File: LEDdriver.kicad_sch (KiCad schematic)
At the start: 5 parts, among them Q30 LBSS84LT1G, Q31 2N7002

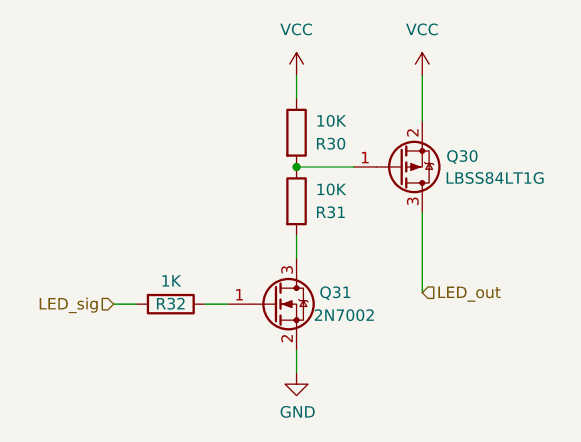
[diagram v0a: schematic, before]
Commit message: Converted Project name to Rotini + files ordered for V1
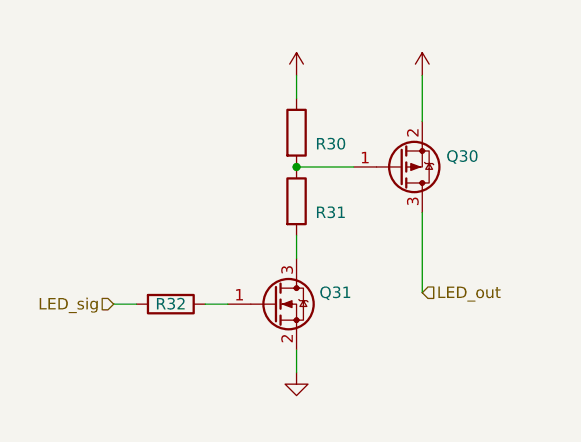
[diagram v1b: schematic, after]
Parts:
- Q30: value LBSS84LT1G -> (none); footprint Package_TO_SOT_SMD:SOT-23 -> (none)
- Q31: value 2N7002 -> (none); footprint Package_TO_SOT_SMD:SOT-23 -> (none)
- R30, R31: value 10K -> (none); footprint Resistor_SMD:R_0402_1005Metric -> (none)
- R32: value 1K -> (none); footprint Resistor_SMD:R_0402_1005Metric -> (none)
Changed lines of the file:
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@@
   (symbol (lib_id "power:VCC") (at 139.7 86.36 0) (unit 1)
     (in_bom yes) (on_board yes) (fields_autoplaced)
-    (property "Reference" "#PWR0175" (id 0) (at 139.7 90.17 0)
+    (property "Reference" "#PWR0152" (id 0) (at 139.7 90.17 0)
       (effects (font (size 1.27 1.27)) hide)
     )
-    (property "Value" "VCC" (id 1) (at 139.7 81.28 0))
+    (property "Value" "" (id 1) (at 139.7 81.28 0))
     (property "Footprint" "" (id 2) (at 139.7 86.36 0)
       (effects (font (size 1.27 1.27)) hide)
@@
       (effects (font (size 1.27 1.27)) (justify left))
     )
-    (property "Value" "2N7002" (id 1) (at 141.605 113.03 0)
+    (property "Value" "" (id 1) (at 141.605 113.03 0)
       (effects (font (size 1.27 1.27)) (justify left))
     )
-    (property "Footprint" "Package_TO_SOT_SMD:SOT-23" (id 2) (at 142.24 113.665 0)
+    (property "Footprint" "" (id 2) (at 142.24 113.665 0)
       (effects (font (size 1.27 1.27) italic) (justify left) hide)
     )
@@
     (in_bom yes) (on_board yes)
     (property "Reference" "R31" (id 0) (at 143.51 101.6 0))
-    (property "Value" "10K" (id 1) (at 143.51 99.06 0))
-    (property "Footprint" "Resistor_SMD:R_0402_1005Metric" (id 2) (at 137.922 100.33 90)
+    (property "Value" "" (id 1) (at 143.51 99.06 0))
+    (property "Footprint" "" (id 2) (at 137.922 100.33 90)
       (effects (font (size 1.27 1.27)) hide)
     )
@@
   (symbol (lib_id "power:GND") (at 139.7 119.38 0) (unit 1)
     (in_bom yes) (on_board yes)
-    (property "Reference" "#PWR0174" (id 0) (at 139.7 125.73 0)
+    (property "Reference" "#PWR0121" (id 0) (at 139.7 125.73 0)
       (effects (font (size 1.27 1.27)) hide)
     )
-    (property "Value" "GND" (id 1) (at 139.827 123.7742 0))
+    (property "Value" "" (id 1) (at 139.827 123.7742 0))
     (property "Footprint" "" (id 2) (at 139.7 119.38 0)
       (effects (font (size 1.27 1.27)) hide)
@@
       (effects (font (size 1.27 1.27)) (justify left))
     )
-    (property "Value" "LBSS84LT1G" (id 1) (at 156.21 97.79 0)
+    (property "Value" "" (id 1) (at 156.21 97.79 0)
       (effects (font (size 1.27 1.27)) (justify left))
     )
-    (property "Footprint" "Package_TO_SOT_SMD:SOT-23" (id 2) (at 156.21 94.615 0)
+    (property "Footprint" "" (id 2) (at 156.21 94.615 0)
       (effects (font (size 1.27 1.27) italic) (justify left) hide)
     )
@@
     (in_bom yes) (on_board yes)
     (property "Reference" "R30" (id 0) (at 143.51 93.98 0))
-    (property "Value" "10K" (id 1) (at 143.51 91.44 0))
-    (property "Footprint" "Resistor_SMD:R_0402_1005Metric" (id 2) (at 137.922 92.71 90)
+    (property "Value" "" (id 1) (at 143.51 91.44 0))
+    (property "Footprint" "" (id 2) (at 137.922 92.71 90)
       (effects (font (size 1.27 1.27)) hide)
     )
@@
     (in_bom yes) (on_board yes)
     (property "Reference" "R32" (id 0) (at 125.73 111.76 90))
-    (property "Value" "1K" (id 1) (at 125.73 109.22 90))
-    (property "Footprint" "Resistor_SMD:R_0402_1005Metric" (id 2) (at 125.73 109.982 90)
+    (property "Value" "" (id 1) (at 125.73 109.22 90))
+    (property "Footprint" "" (id 2) (at 125.73 109.982 90)
       (effects (font (size 1.27 1.27)) hide)
     )
@@
   (symbol (lib_id "power:VCC") (at 153.67 86.36 0) (unit 1)
     (in_bom yes) (on_board yes) (fields_autoplaced)
-    (property "Reference" "#PWR0176" (id 0) (at 153.67 90.17 0)
+    (property "Reference" "#PWR0122" (id 0) (at 153.67 90.17 0)
       (effects (font (size 1.27 1.27)) hide)
     )
-    (property "Value" "VCC" (id 1) (at 153.67 81.28 0))
+    (property "Value" "" (id 1) (at 153.67 81.28 0))
     (property "Footprint" "" (id 2) (at 153.67 86.36 0)
       (effects (font (size 1.27 1.27)) hide)

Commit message: First push with Rotini V2 features, removed CP210x USB circuit
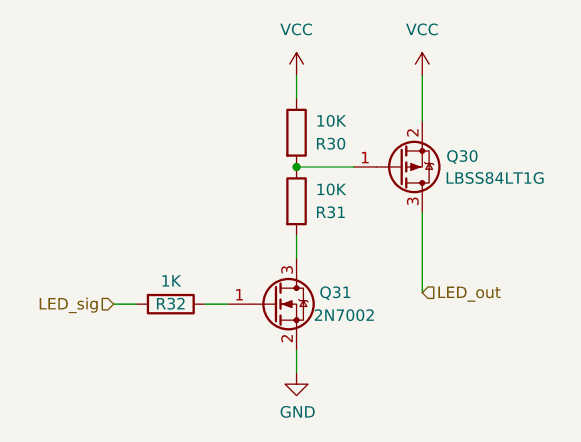
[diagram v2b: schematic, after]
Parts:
- Q30: value (none) -> LBSS84LT1G
- Q31: value (none) -> 2N7002
- R30, R31: value (none) -> 10K
- R32: value (none) -> 1K
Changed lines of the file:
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@@
       (effects (font (size 1.27 1.27)) hide)
     )
-    (property "Value" "" (id 1) (at 139.7 81.28 0))
+    (property "Value" "VCC" (id 1) (at 139.7 81.28 0))
     (property "Footprint" "" (id 2) (at 139.7 86.36 0)
       (effects (font (size 1.27 1.27)) hide)
@@
       (effects (font (size 1.27 1.27)) (justify left))
     )
-    (property "Value" "" (id 1) (at 141.605 113.03 0)
+    (property "Value" "2N7002" (id 1) (at 141.605 113.03 0)
       (effects (font (size 1.27 1.27)) (justify left))
     )
@@
     (in_bom yes) (on_board yes)
     (property "Reference" "R31" (id 0) (at 143.51 101.6 0))
-    (property "Value" "" (id 1) (at 143.51 99.06 0))
+    (property "Value" "10K" (id 1) (at 143.51 99.06 0))
     (property "Footprint" "" (id 2) (at 137.922 100.33 90)
       (effects (font (size 1.27 1.27)) hide)
@@
       (effects (font (size 1.27 1.27)) hide)
     )
-    (property "Value" "" (id 1) (at 139.827 123.7742 0))
+    (property "Value" "GND" (id 1) (at 139.827 123.7742 0))
     (property "Footprint" "" (id 2) (at 139.7 119.38 0)
       (effects (font (size 1.27 1.27)) hide)
@@
       (effects (font (size 1.27 1.27)) (justify left))
     )
-    (property "Value" "" (id 1) (at 156.21 97.79 0)
+    (property "Value" "LBSS84LT1G" (id 1) (at 156.21 97.79 0)
       (effects (font (size 1.27 1.27)) (justify left))
     )
@@
     (in_bom yes) (on_board yes)
     (property "Reference" "R30" (id 0) (at 143.51 93.98 0))
-    (property "Value" "" (id 1) (at 143.51 91.44 0))
+    (property "Value" "10K" (id 1) (at 143.51 91.44 0))
     (property "Footprint" "" (id 2) (at 137.922 92.71 90)
       (effects (font (size 1.27 1.27)) hide)
@@
     (in_bom yes) (on_board yes)
     (property "Reference" "R32" (id 0) (at 125.73 111.76 90))
-    (property "Value" "" (id 1) (at 125.73 109.22 90))
+    (property "Value" "1K" (id 1) (at 125.73 109.22 90))
     (property "Footprint" "" (id 2) (at 125.73 109.982 90)
       (effects (font (size 1.27 1.27)) hide)
@@
       (effects (font (size 1.27 1.27)) hide)
     )
-    (property "Value" "" (id 1) (at 153.67 81.28 0))
+    (property "Value" "VCC" (id 1) (at 153.67 81.28 0))
     (property "Footprint" "" (id 2) (at 153.67 86.36 0)
       (effects (font (size 1.27 1.27)) hide)

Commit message: Hardware bought of Rotini V2
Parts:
- Q30, Q31: footprint (none) -> Package_TO_SOT_SMD:SOT-23
- R30, R31, R32: footprint (none) -> Resistor_SMD:R_0402_1005Metric
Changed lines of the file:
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@@
       (effects (font (size 1.27 1.27)) (justify left))
     )
-    (property "Footprint" "" (id 2) (at 142.24 113.665 0)
+    (property "Footprint" "Package_TO_SOT_SMD:SOT-23" (id 2) (at 142.24 113.665 0)
       (effects (font (size 1.27 1.27) italic) (justify left) hide)
     )
@@
     (property "Reference" "R31" (id 0) (at 143.51 101.6 0))
     (property "Value" "10K" (id 1) (at 143.51 99.06 0))
-    (property "Footprint" "" (id 2) (at 137.922 100.33 90)
+    (property "Footprint" "Resistor_SMD:R_0402_1005Metric" (id 2) (at 137.922 100.33 90)
       (effects (font (size 1.27 1.27)) hide)
     )
@@
       (effects (font (size 1.27 1.27)) (justify left))
     )
-    (property "Footprint" "" (id 2) (at 156.21 94.615 0)
+    (property "Footprint" "Package_TO_SOT_SMD:SOT-23" (id 2) (at 156.21 94.615 0)
       (effects (font (size 1.27 1.27) italic) (justify left) hide)
     )
@@
     (property "Reference" "R30" (id 0) (at 143.51 93.98 0))
     (property "Value" "10K" (id 1) (at 143.51 91.44 0))
-    (property "Footprint" "" (id 2) (at 137.922 92.71 90)
+    (property "Footprint" "Resistor_SMD:R_0402_1005Metric" (id 2) (at 137.922 92.71 90)
       (effects (font (size 1.27 1.27)) hide)
     )
@@
     (property "Reference" "R32" (id 0) (at 125.73 111.76 90))
     (property "Value" "1K" (id 1) (at 125.73 109.22 90))
-    (property "Footprint" "" (id 2) (at 125.73 109.982 90)
+    (property "Footprint" "Resistor_SMD:R_0402_1005Metric" (id 2) (at 125.73 109.982 90)
       (effects (font (size 1.27 1.27)) hide)
     )

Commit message: Cleaned up schematic
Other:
- title: (none) -> LED Driver
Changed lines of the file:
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@@
 (kicad_sch (version 20211123) (generator eeschema)
   (paper "A4")
+  (title_block
+    (title "LED Driver")
+  )
   (junction (at 139.7 96.52) (diameter 0) (color 0 0 0 0)
   )
